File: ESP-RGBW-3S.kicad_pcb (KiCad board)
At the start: 2 copper layers, 66.7 x 48.3 mm, 38 parts, among them J1 12V IN, J2 PROG, J3 LED Str., J4 Temp. S., J5 Light. S., J6 PIR, Q1 IRLL024NPBF, Q2 IRLL024NPBF, Q3 IRLL024NPBF, Q4 IRLL024NPBF, SW1 Flash, U2 ESP-12E, U4 DCDC_LM2596

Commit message: v 0.2
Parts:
- C1, C2: footprint Capacitor_SMD:C_0805_2012Metric_Pad1.15x1.40mm_HandSolder -> Capacitor_SMD:C_0805_2012Metric
- Q1, Q2, Q3, Q4: value IRLL024NPBF -> IRLML0040TRPBF; footprint Package_TO_SOT_SMD:SOT-23_Handsoldering -> Package_TO_SOT_SMD:SOT-23
- R1, R10, R11, R12, R13, R14, R15, R16, R17, R18, R2, R3, R4, R5, R6, R7, R8, R9: footprint Resistor_SMD:R_0805_2012Metric_Pad1.20x1.40mm_HandSolder -> Resistor_SMD:R_0805_2012Metric
- moved J3 10.2 mm to (25.1, 32.8), turned to 270 degrees
- moved R1 7.94 mm to (61.8, 34.3), turned to 180 degrees
- moved R3 7.94 mm to (61.8, 46.3), turned to 180 degrees
- moved R4 7.94 mm to (61.8, 43.3), turned to 180 degrees
- moved R5 7.94 mm to (61.8, 40.3), turned to 180 degrees
- moved R6 7.94 mm to (61.8, 37.3), turned to 180 degrees
- moved J5 5.09 mm to (25.1, 48.0), turned to 270 degrees
- moved R18 2.20 mm to (35.7, 29.0), turned to 180 degrees
- moved R12 2.03 mm to (43.6, 35.6), turned to 180 degrees
- moved R13 2.03 mm to (43.6, 41.9), turned to 180 degrees
- moved R14 2.03 mm to (43.6, 48.3), turned to 180 degrees
- moved Q4 1.80 mm to (30.1, 28.2)
- moved Q1 1.27 mm to (33.1, 47.5)
- moved Q2 1.27 mm to (33.1, 41.1)
- moved Q3 1.27 mm to (33.1, 34.8)
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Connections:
- net /Blue renamed Red
- net /Green renamed White
- net /Red renamed Blue
- Q1 pad 3: /G-Out -> /W-Out
- Q2 pad 3: /R-Out -> /B-Out
- Q3 pad 3: /B-Out -> /R-Out
- Q4 pad 3: /W-Out -> /G-Out
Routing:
- net +12V: track 35.5 -> 47.9 mm
- net +3V3: track 155.2 -> 165.1 mm, vias 1 -> 0
- net White: track 13.1 -> 6.82 mm
- net Blue: track 11.8 -> 7.92 mm
- net Net-(Q3-Pad1): track 8.29 -> 11.8 mm
- net Net-(Q2-Pad1): track 8.29 -> 11.7 mm
- net Net-(Q1-Pad1): track 8.29 -> 11.7 mm
- net Net-(Q4-Pad1): track 8.29 -> 11.6 mm
- net Red: track 12.8 -> 10.8 mm
- net Net-(R1-Pad2): track 14.0 -> 15.8 mm
- net /B-Out: track 5.43 -> 6.82 mm
- net Net-(R4-Pad2): track 15.1 -> 14.0 mm
- net /SCL: track 29.9 -> 30.9 mm
- net /LED: track 12.0 -> 12.9 mm
- net /G-Out: track 10.1 -> 9.41 mm
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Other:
- board text added: "Temp/Hum"
- board text removed: "+3.3"
- board text removed: "Temp/Humid"

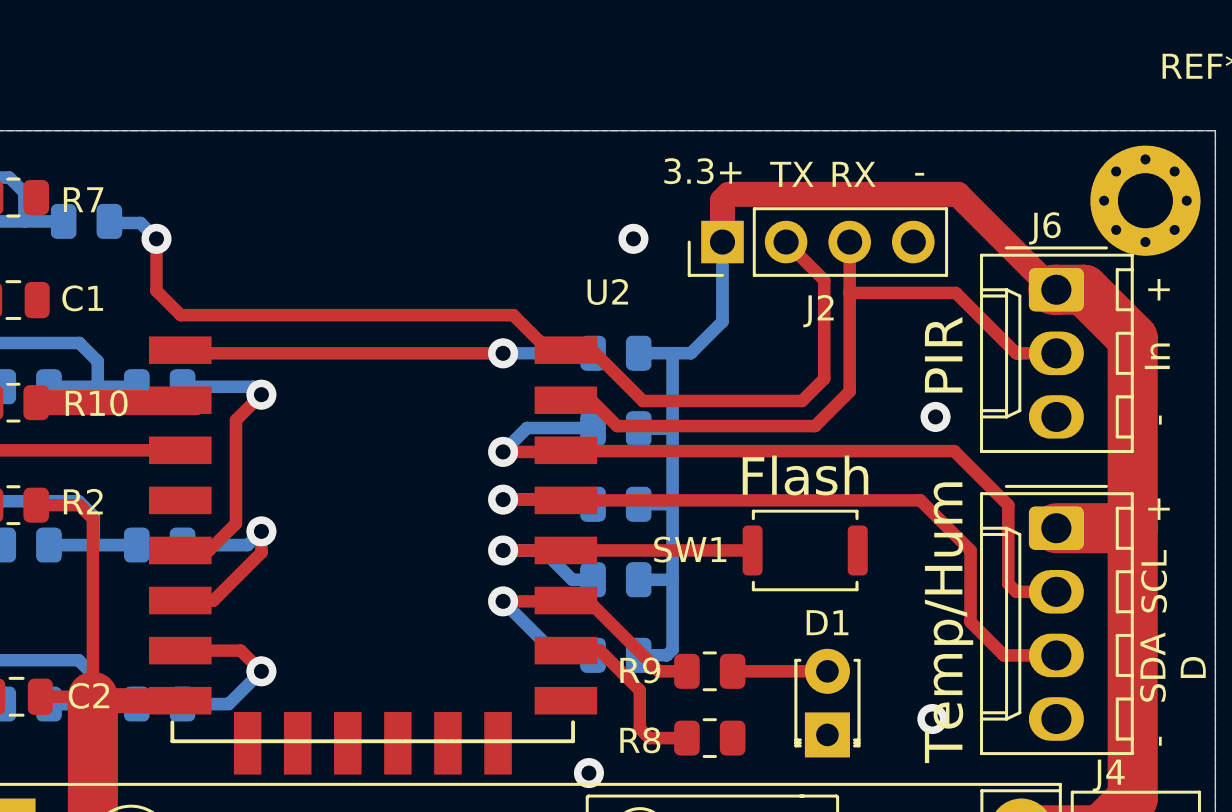
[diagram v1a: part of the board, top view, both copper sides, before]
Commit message: GPIO15 as Red ch. output instead of TX
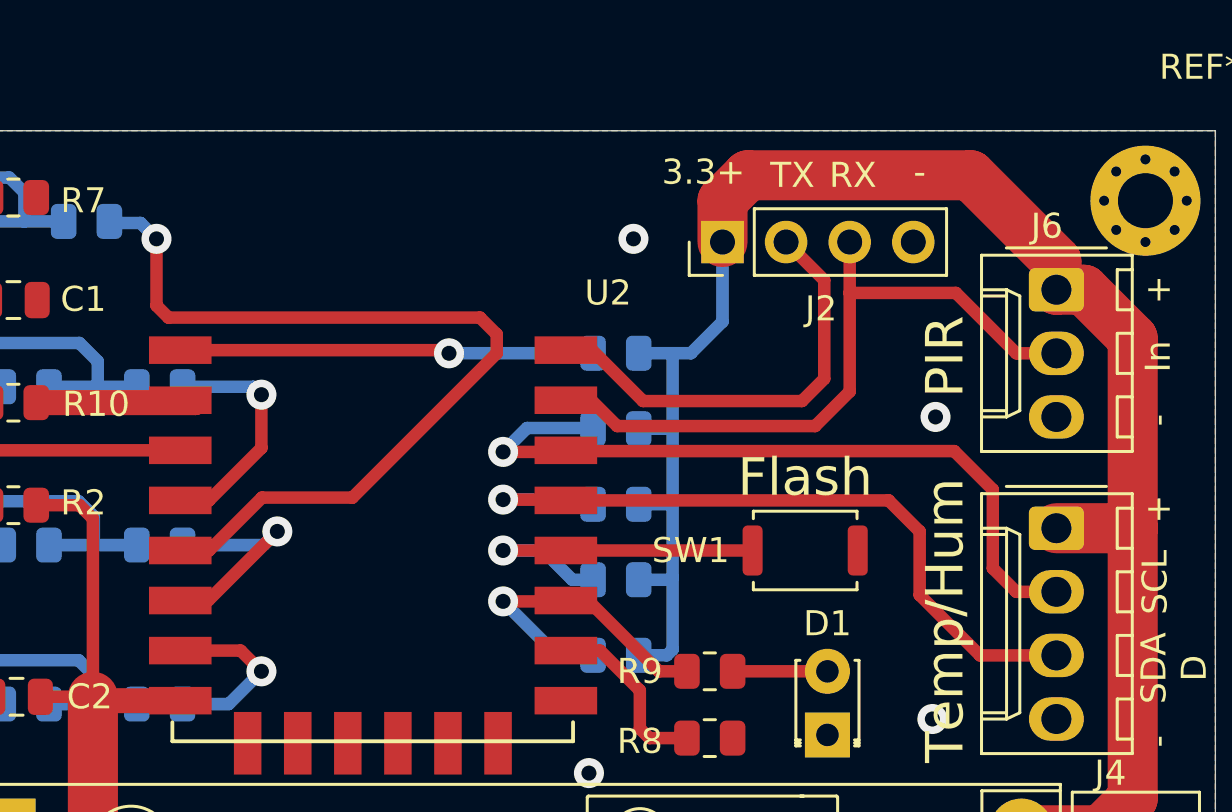
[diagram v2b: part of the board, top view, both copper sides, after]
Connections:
- R11 pad 1: TXD -> Green
- U2 pad 4: Net-(U2-Pad4) -> Red
- U2 pad 5: Red -> Green
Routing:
- net Green: track 0.00 -> 35.0 mm, vias 0 -> 1
- net TXD: track 39.4 -> 18.3 mm, vias 1 -> 0
- net Red: track 10.8 -> 8.82 mm
- net +3V3: track 165.1 -> 166.4 mm

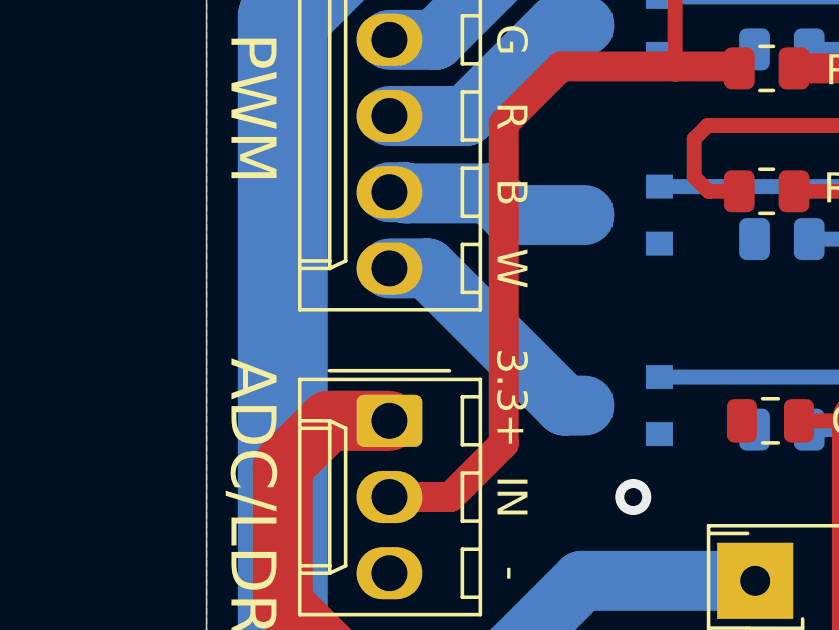
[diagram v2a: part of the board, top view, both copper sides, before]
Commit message: extra GND pin next to PWM
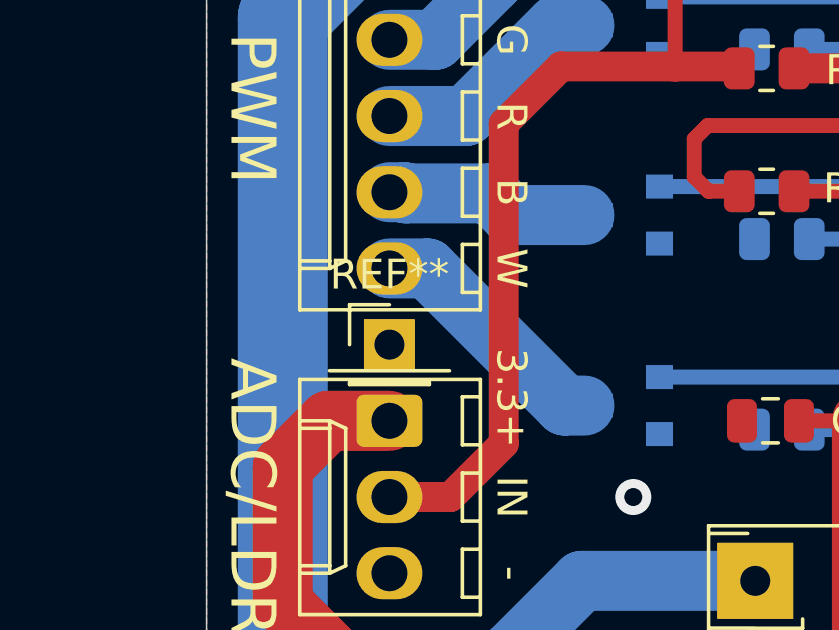
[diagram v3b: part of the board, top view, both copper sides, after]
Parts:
- added REF**: PinHeader_1x01_P2.54mm_Vertical, Connector_PinHeader_2.54mm:PinHeader_1x01_P2.54mm_Vertical, F.Cu at (25.1, 45.5)
